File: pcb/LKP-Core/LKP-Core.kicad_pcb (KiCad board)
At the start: 2 copper layers, 41 x 35 mm, 34 parts, among them J1 Intercon L, J2 Intercon R, J3 Power JST PH, J4 IO, J5 SWD, J6 WS281x, U1 CY8C4246AZI-M445

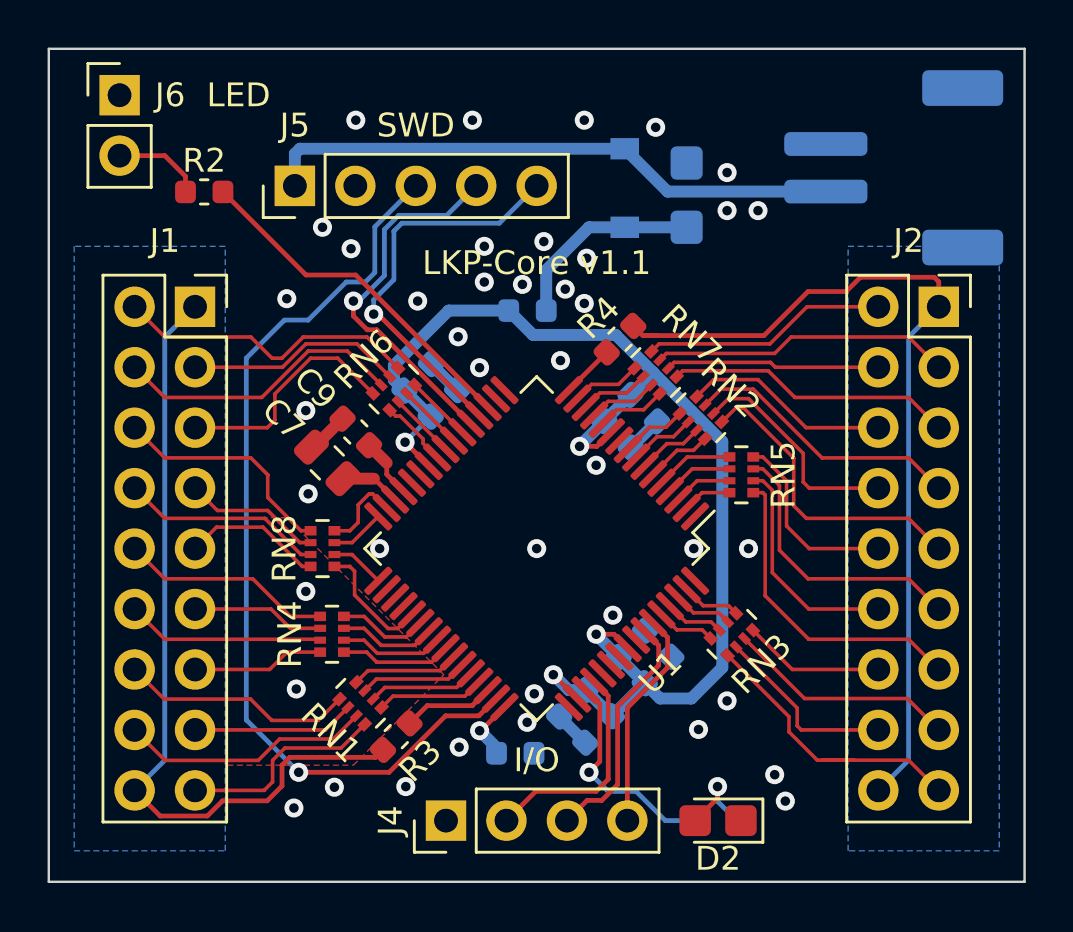
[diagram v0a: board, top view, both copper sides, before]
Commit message: LKP-Core: Add more descriptive silkscreens.
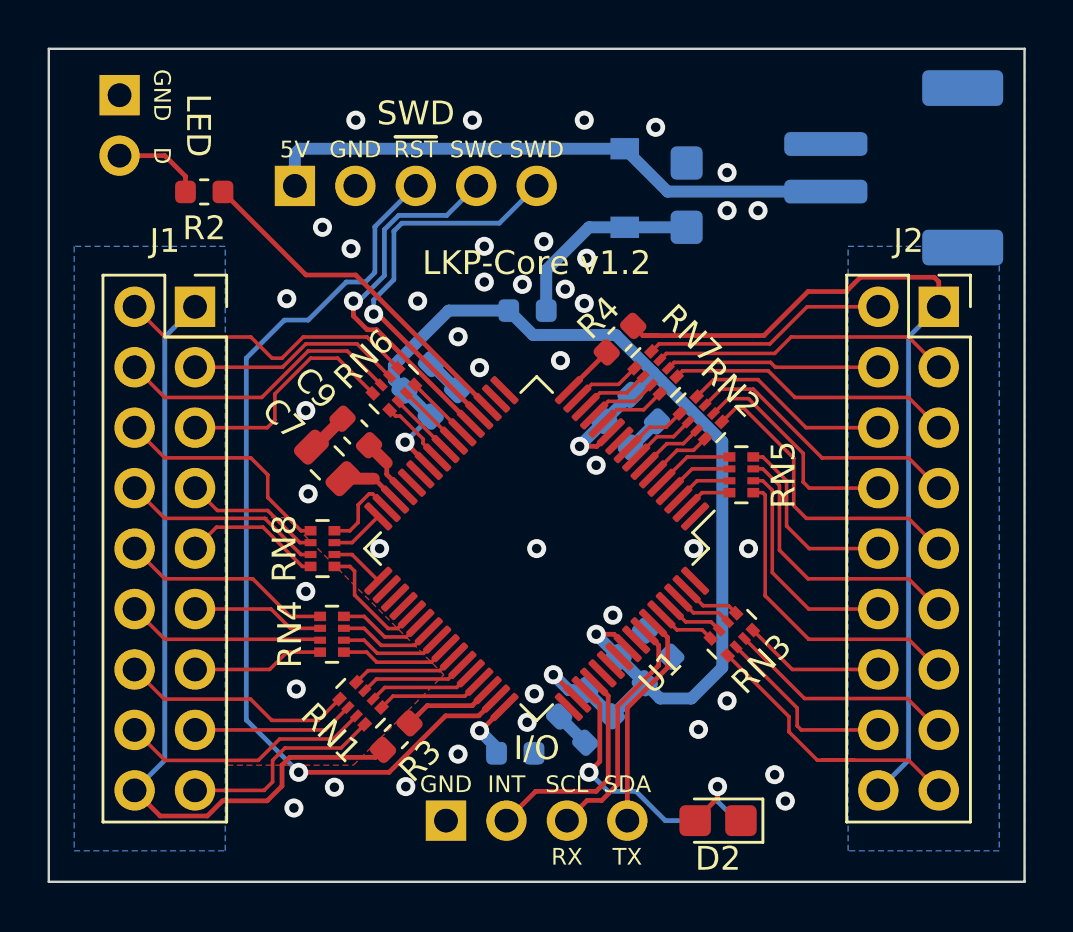
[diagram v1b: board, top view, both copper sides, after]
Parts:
- J4, J5, J6: moved to B.Cu
- turned J4 to 270 degrees
- turned J5 to 270 degrees
- turned J6 to 180 degrees
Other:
- board text added: "+"
- board text added: "D"
- board text added: "GND"
- board text added: "INT"
- board text added: "LKP-Core v1.2"
- board text added: "RX"
- board text added: "SCL"
- board text added: "SDA"
- board text added: "SWC"
- board text added: "TX"
- board text added: "~RST"
- board text removed: "LKP-Core v1.1"

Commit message: D -> DO
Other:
- board text added: "DO"
- board text removed: "D"

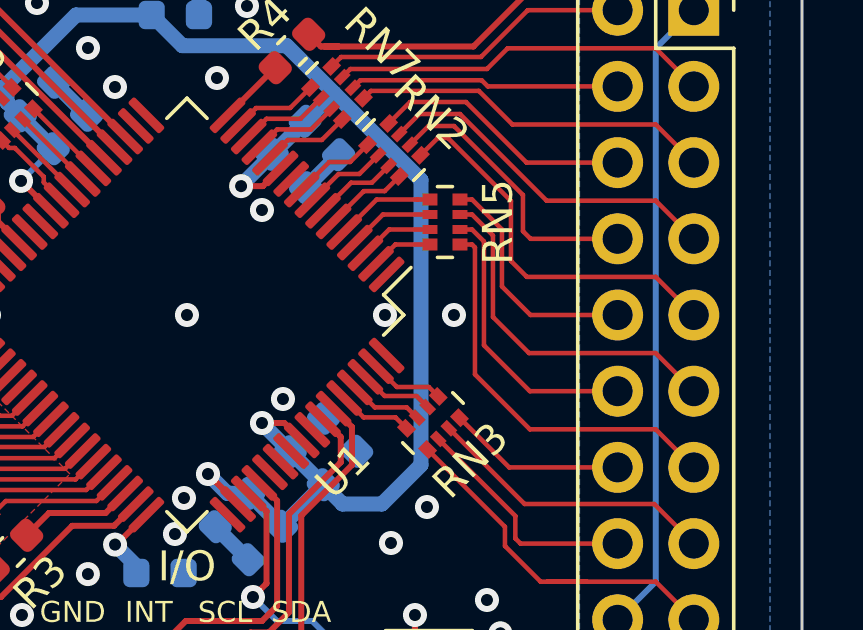
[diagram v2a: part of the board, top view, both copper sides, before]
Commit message: LKP-Core: Change minimum mask width and clearance to 0. Slight GND via rearrangements.
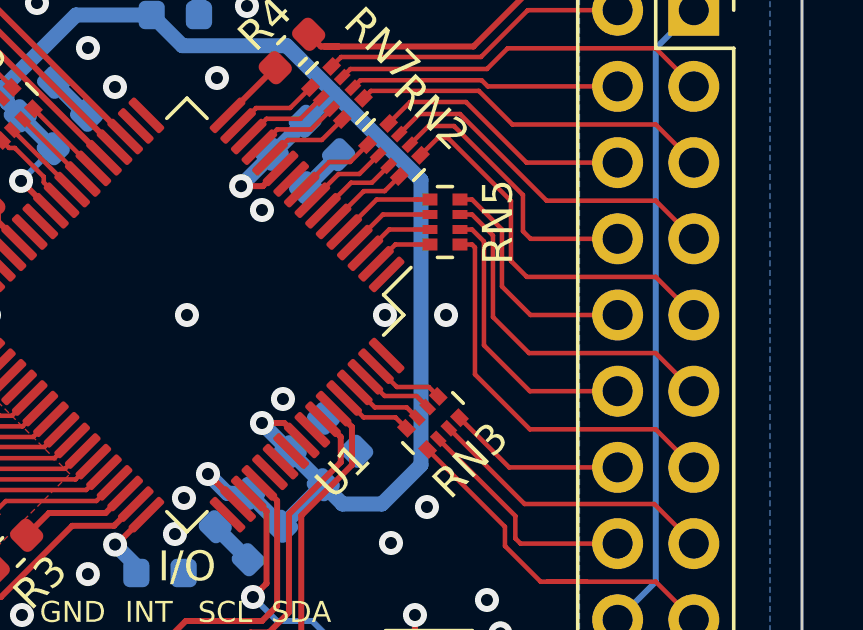
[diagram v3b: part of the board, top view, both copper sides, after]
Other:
- rule pad_to_mask_clearance: 0.05 -> 0
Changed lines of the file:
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@@
     (pad_size 1.524 1.524)
     (pad_drill 0.762)
-    (pad_to_mask_clearance 0.05)
-    (solder_mask_min_width 0.0762)
+    (pad_to_mask_clearance 0)
     (aux_axis_origin 0 0)
     (grid_origin 146.875 98)
@@
   (via (at 141.875 87.6) (size 0.8) (drill 0.4) (layers F.Cu B.Cu) (net 1))
   (via (at 136.675 108.9) (size 0.8) (drill 0.4) (layers F.Cu B.Cu) (net 1))
-  (via (at 155.775 98) (size 0.8) (drill 0.4) (layers F.Cu B.Cu) (net 1))
+  (via (at 155.511 98) (size 0.8) (drill 0.4) (layers F.Cu B.Cu) (net 1))
   (segment (start 137.212087 93.837087) (end 137.424219 93.837087) (width 0.5) (layer F.Cu) (net 1) (status 30))
   (via (at 146.475 105.3) (size 0.8) (drill 0.4) (layers F.Cu B.Cu) (net 1))
